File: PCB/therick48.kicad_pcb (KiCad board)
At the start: 2 copper layers, 226.5 x 75.8 mm, 132 parts, among them J1 TYPE-C-31-M12_13, J2 AVR-ISP-6_mod, K1 KEYSW, K10 KEYSW, K11 KEYSW, K12 KEYSW, K13 KEYSW, K14 KEYSW, K15 KEYSW, K16 KEYSW, K17 KEYSW, K18 KEYSW, K19 KEYSW, K2 KEYSW, K20 KEYSW, K21 KEYSW, K22 KEYSW, K23 KEYSW, K24 KEYSW, K25 KEYSW, K26 KEYSW, K27 KEYSW, K28 KEYSW, K29 KEYSW, K3 KEYSW, K30 KEYSW, K31 KEYSW, K32 KEYSW, K33 KEYSW, K34 KEYSW, K35 KEYSW, K36 KEYSW, K37 KEYSW, K38 KEYSW, K39 KEYSW, K4 KEYSW, K40 KEYSW, K41 KEYSW, K42 KEYSW, K43 KEYSW, K44 KEYSW, K45 KEYSW, K46 KEYSW, K47 KEYSW, K48 KEYSW, K5 KEYSW, K6 KEYSW, K7 KEYSW, K8 KEYSW, K9 KEYSW, SW1 SW_PUSH, U1 ATMEGA32U4, U2 HOLE, U3 USBLC6-2SC6, Y1 16MHz

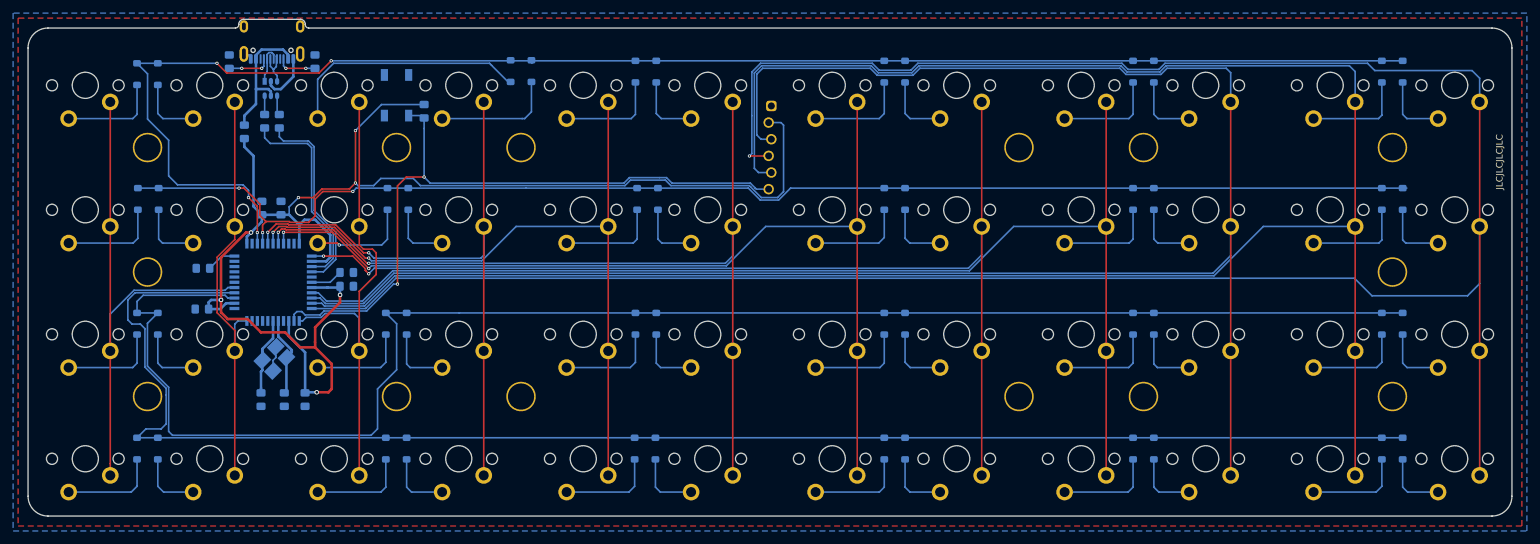
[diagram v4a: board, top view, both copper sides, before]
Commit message: Move mounting holes to PCB
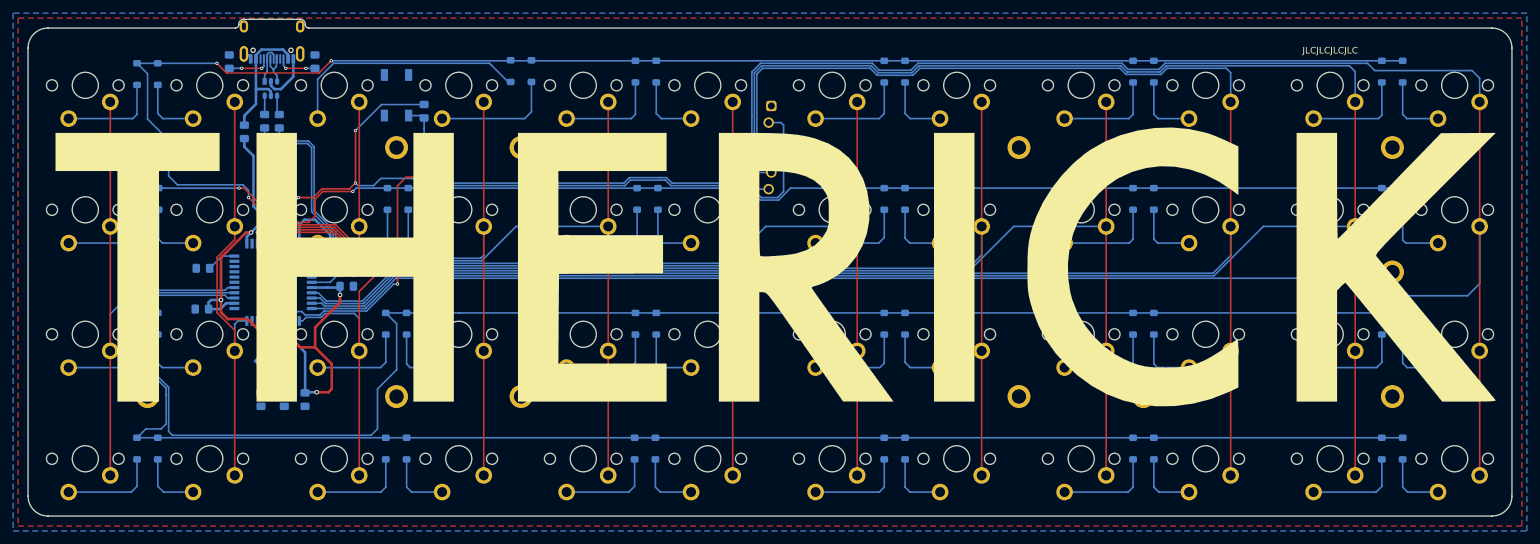
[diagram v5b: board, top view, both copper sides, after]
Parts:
- added U4: HOLE, Artwork:THERICK, F.Cu at (160.0, 73.0)
- H1, H10, H11, H12, H13, H14, H2, H3, H4, H5, H6, H7, H8, H9: footprint random-keyboard-parts:plate_hole_4mm_tht -> random-keyboard-parts:Generic-Mounthole
- moved H1 2.03 mm to (65.0, 73.0)
- moved H10 2.03 mm to (122.0, 92.0)
- moved H3 2.03 mm to (103.0, 92.0)
- moved H9 2.03 mm to (65.0, 92.0)
- moved H11 2.03 mm to (255.0, 92.0)
- moved H12 2.03 mm to (198.0, 92.0)
- moved H5 2.03 mm to (217.0, 92.0)
- moved H6 2.03 mm to (255.0, 73.0)
- moved H13 2.03 mm to (122.0, 54.0)
- moved H2 2.03 mm to (103.0, 54.0)
- moved H7 2.03 mm to (65.0, 54.0)
- moved H14 2.03 mm to (198.0, 54.0)
- moved H4 2.03 mm to (217.0, 54.0)
- moved H8 2.03 mm to (255.0, 54.0)
